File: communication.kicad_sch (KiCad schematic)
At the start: 8 parts, among them Y1 16MHz

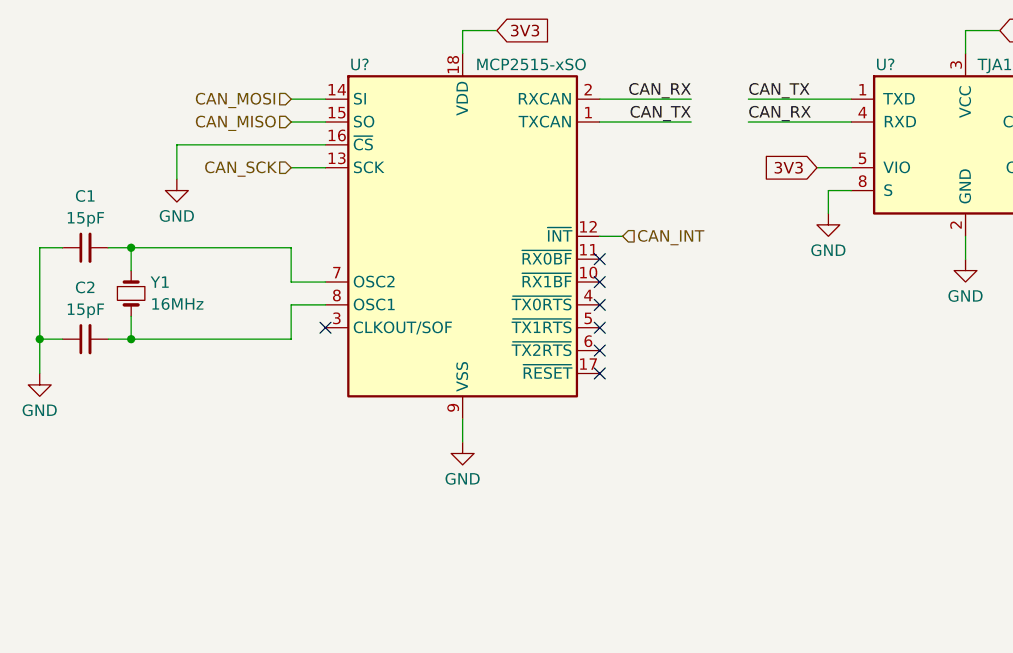
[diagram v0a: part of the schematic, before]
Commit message: removed the mcp2515 can controller because I can use the can2040 library instead
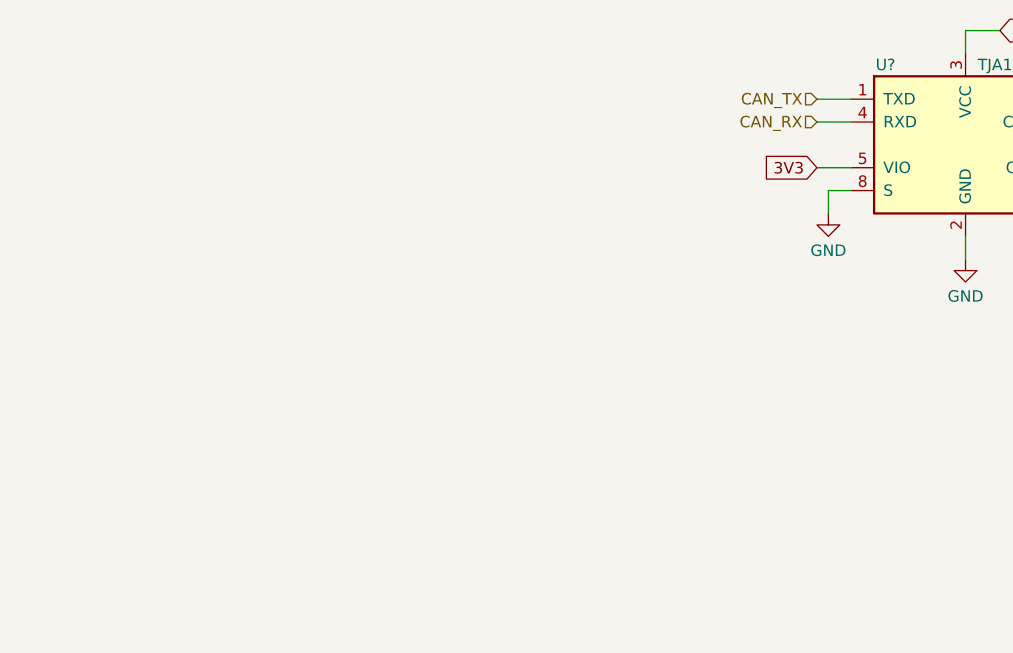
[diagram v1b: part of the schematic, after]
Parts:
- removed C1, C2: 15pF, Capacitor_SMD:C_0402_1005Metric_Pad0.74x0.62mm_HandSolder, symbol Device:C_Small
- removed U?: MCP2515-xSO, Package_SO:SOIC-18W_7.5x11.6mm_P1.27mm, symbol Interface_CAN_LIN:MCP2515-xSO
- removed Y1: 16MHz, Crystal:Crystal_HC49-U_Vertical, symbol Device:Crystal_Small
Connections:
- no-connect marks 7 -> 0
